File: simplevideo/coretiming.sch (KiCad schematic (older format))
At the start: 9 parts, among them U2 CD74HC40103, U3 CD74HC40103, U6 74HC74, U7 CD74HC40103, U8 CD74HC40103, X1 CXO_DIP8

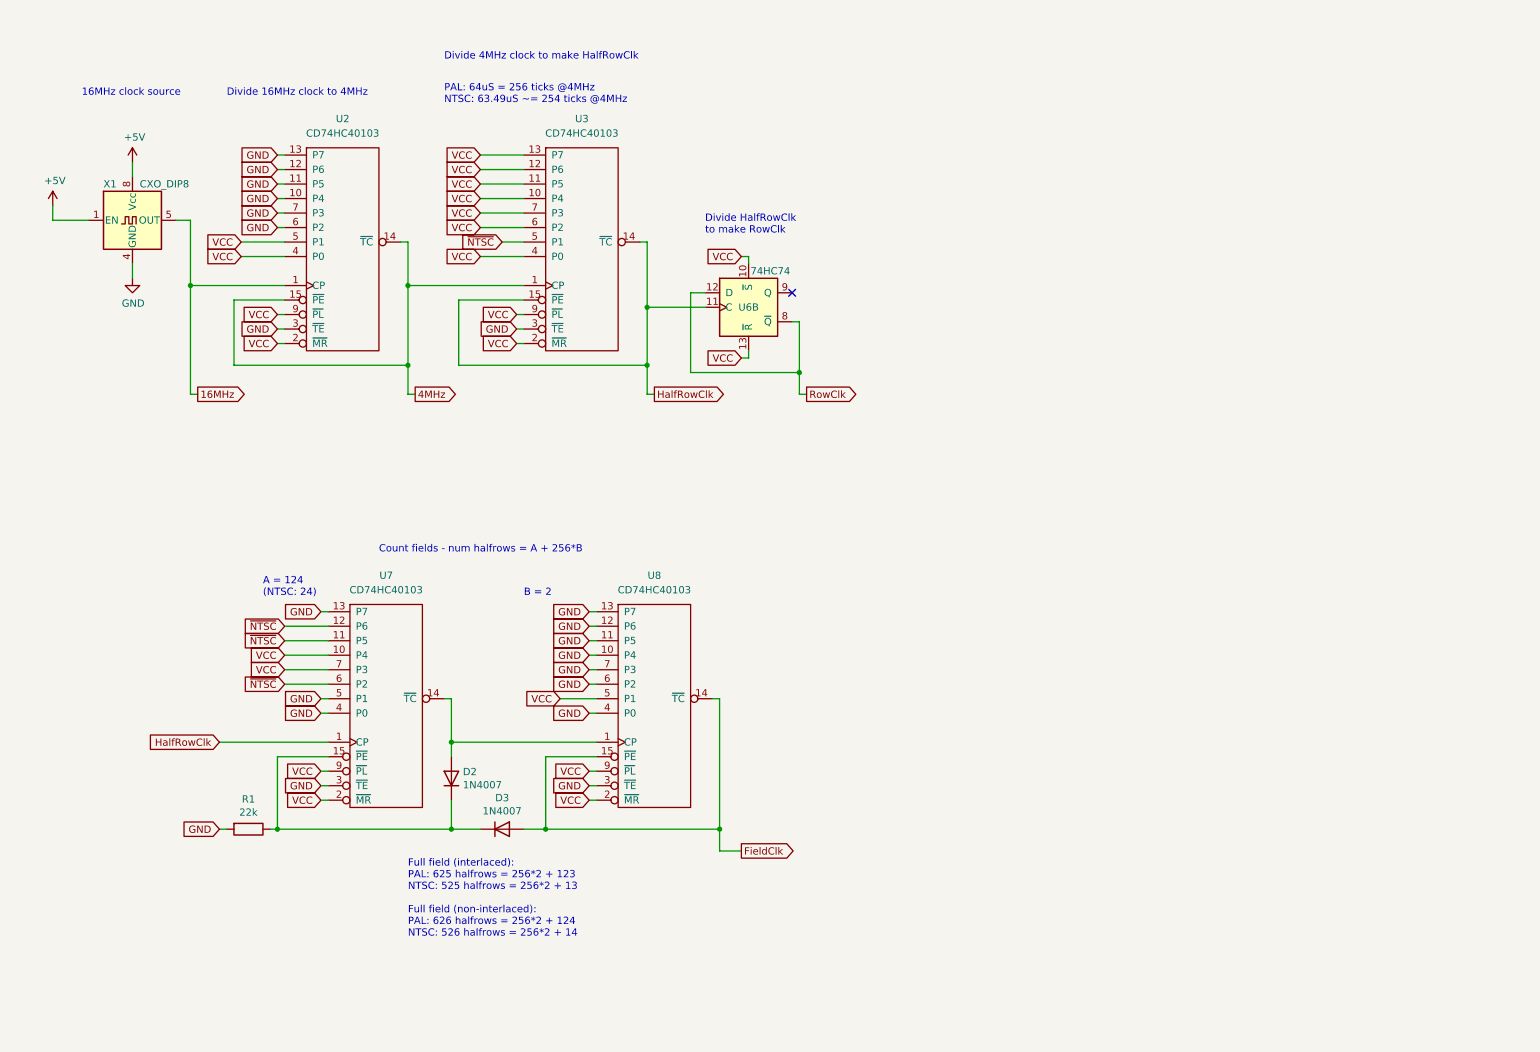
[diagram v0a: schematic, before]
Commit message: Include 6502, ROM, etc in circuit, all laid out together
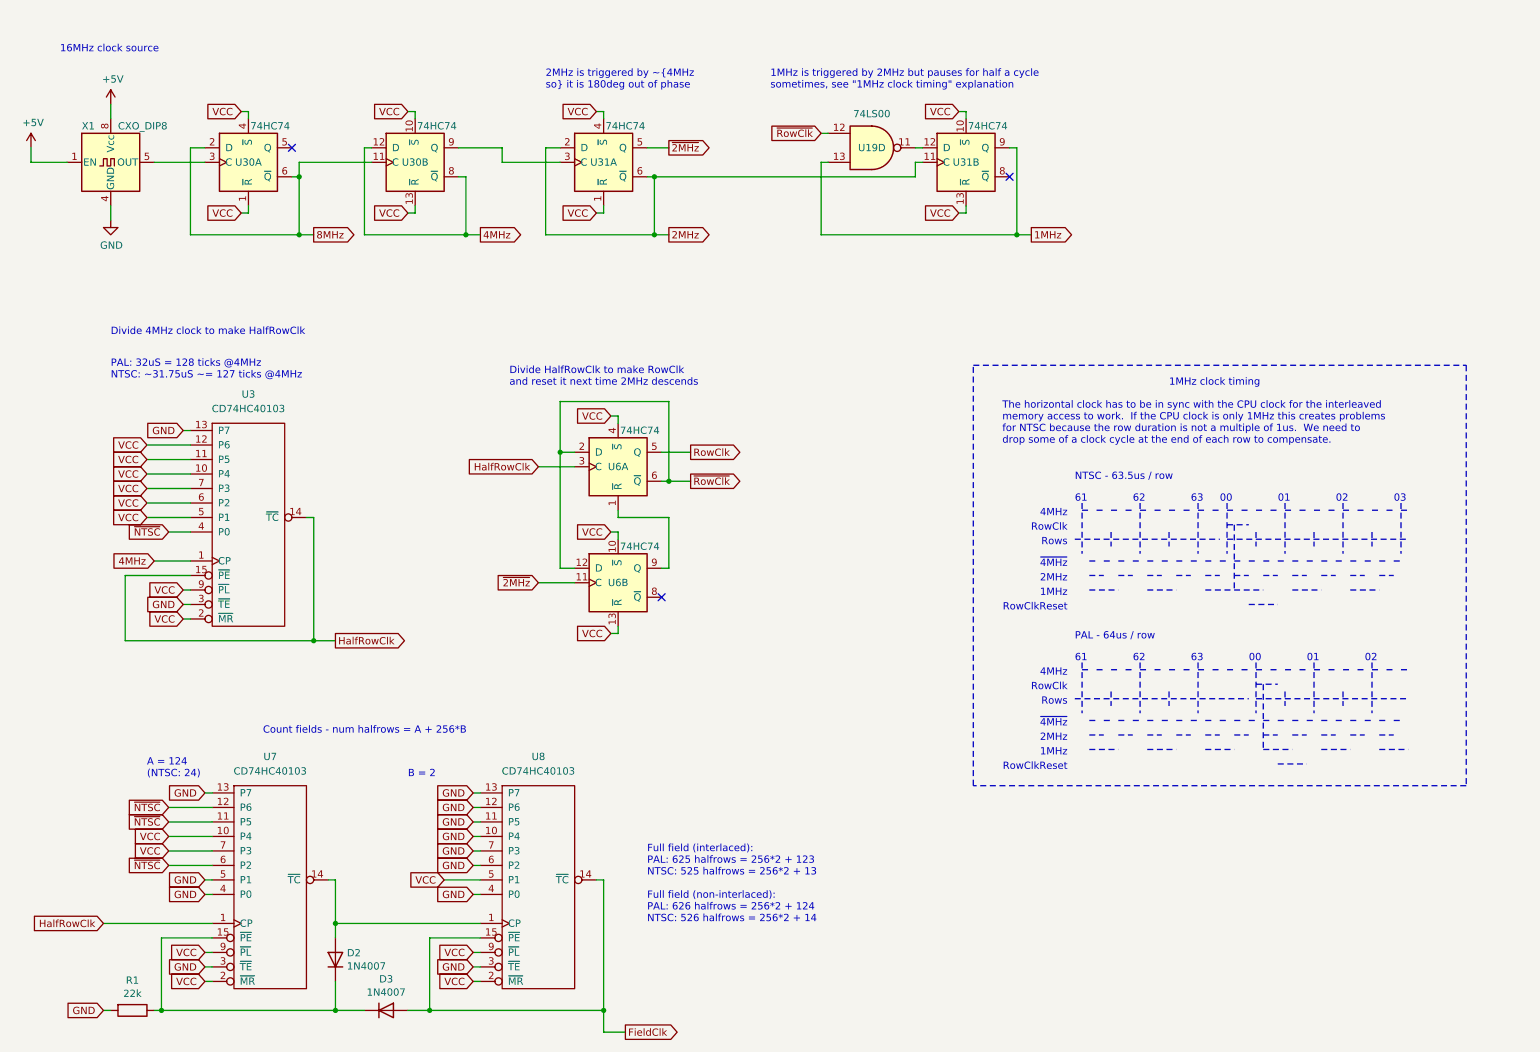
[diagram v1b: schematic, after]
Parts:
- removed U2: CD74HC40103, Package_DIP:DIP-16_W7.62mm, symbol g200kg_CD74HCxx:CD74HC40103
- added U19: 74LS00, Package_DIP:DIP-14_W7.62mm, symbol 74xx:74LS00
- added U30, U31: 74HC74, Package_DIP:DIP-14_W7.62mm, symbol 74xx:74HC74
- added unit 2 of U6
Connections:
- net 4MHz: now also U30.12 (D), U30.8 (~Q)
- net GND: now also U3.13 (P7)
- net HalfRowClk: now also U6.3 (C); no longer U6.11 (C)
- net RowClk: now also U6.5 (Q); no longer U6.12 (D), U6.8 (~Q)
- net VCC: now also U3.5 (P1), U6.4 (~S), U30.1 (~R), U30.10 (~S), U30.13 (~R), U30.4 (~S), U31.1 (~R), U31.10 (~S), U31.13 (~R), U31.4 (~S), U6.10 (~S), U6.13 (~R); no longer U3.13 (P7), U3.4 (P0), U6.10 (~S), U6.13 (~R)
- net ~NTSC: now also U3.4 (P0); no longer U3.5 (P1)
- net 16MHz: no longer names the net of X1.5 (OUT)
- net 16MHz: now also U30.3 (C)
- new net: U6.1 (~R), U6.9 (Q)
- new net: U30.9 (Q), U31.3 (C)
- new net: U19.11, U31.12 (D)
- new net 1MHz: U19.13, U31.9 (Q)
- new net 2MHz: U31.11 (C), U31.2 (D), U31.6 (~Q)
- new net 8MHz: U30.11 (C), U30.2 (D), U30.6 (~Q)
- new net ~2MHz: U31.5 (Q), U6.11 (C)
- new net ~RowClk: U19.12, U6.12 (D), U6.2 (D), U6.6 (~Q)
- no-connect marks 1 -> 3
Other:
- note added: "00"
- note added: "01"
- note added: "02"
- note added: "03"
- note added: "1MHz"
- note added: "1MHz clock timing"
- note added: "1MHz is triggered by 2MHz but pauses for half a cycle\nsometimes, see "1MHz clock timing" explanation"
- note added: "2MHz"
- note added: "2MHz is triggered by ~4MHz\nso it is 180deg out of phase"
- note added: "4MHz"
- note added: "61"
- note added: "62"
- note added: "63"
- note added: "Divide HalfRowClk to make RowClk \nand reset it next time 2MHz descends"
- note added: "NTSC - 63.5us / row"
- note added: "PAL - 64us / row"
- note added: "PAL: 32uS = 128 ticks @4MHz\nNTSC: ~~31.75uS ~~= 127 ticks @4MHz"
- note added: "RowClk"
- note added: "RowClkReset"
- note added: "Rows"
- note added: "The horizontal clock has to be in sync with the CPU clock for the interleaved \nmemory access to work. If the CPU clock is only 1MHz this creates problems\nfor NTSC because the row duration is not a multiple of 1us. We need to \ndrop some of a clock cycle at the end of each row to compensate."
- note added: "~4MHz"
- note removed: "Divide 16MHz clock to 4MHz"
- note removed: "Divide HalfRowClk\nto make RowClk"
- note removed: "PAL: 64uS = 256 ticks @4MHz\nNTSC: 63.49uS ~~= 254 ticks @4MHz"
- moved on the sheet: D2, D3, R1, U3, U7, U8, X1

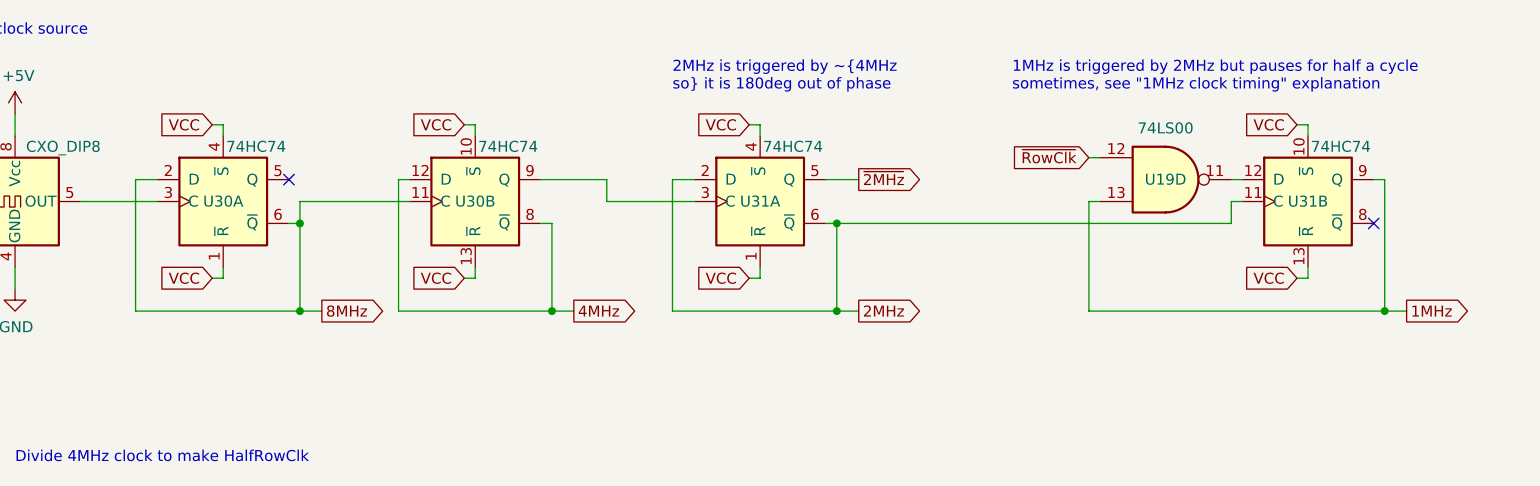
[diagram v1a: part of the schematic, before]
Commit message: New address decoding scheme and complete breadboard layout, should be ready to build
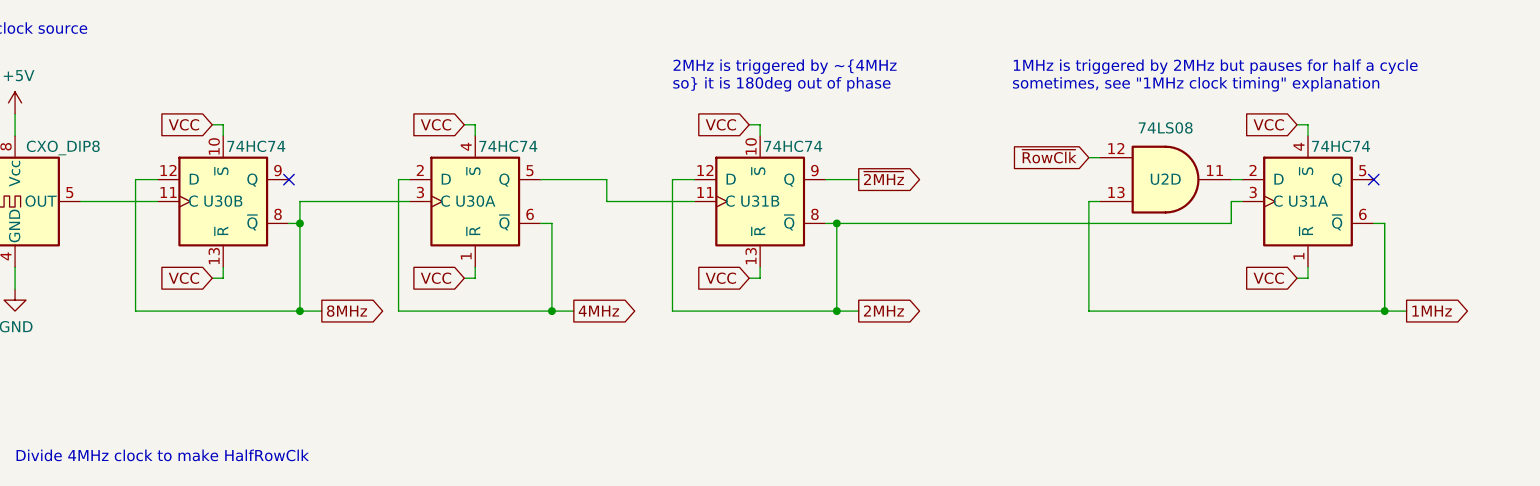
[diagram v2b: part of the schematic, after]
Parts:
- removed U19: 74LS00, Package_DIP:DIP-14_W7.62mm, symbol 74xx:74LS00
- added U2: 74LS08, Package_DIP:DIP-14_W7.62mm, symbol 74xx:74LS08
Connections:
- net 1MHz: now also U31.6 (~Q), U2.13; no longer U31.9 (Q)
- net 2MHz: now also U31.12 (D), U31.3 (C), U31.8 (~Q); no longer U31.11 (C), U31.2 (D), U31.6 (~Q)
- net 4MHz: now also U30.2 (D), U30.6 (~Q); no longer U30.12 (D), U30.8 (~Q)
- net 8MHz: now also U30.12 (D), U30.3 (C), U30.8 (~Q); no longer U30.11 (C), U30.2 (D), U30.6 (~Q)
- net VCC: now also U30.1 (~R), U30.10 (~S), U30.13 (~R), U30.4 (~S), U31.1 (~R), U31.10 (~S), U31.13 (~R), U31.4 (~S); no longer U30.1 (~R), U30.10 (~S), U30.13 (~R), U30.4 (~S), U31.1 (~R), U31.10 (~S), U31.13 (~R), U31.4 (~S)
- net ~2MHz: now also U31.9 (Q); no longer U31.5 (Q)
- net ~RowClk: now also U2.12
- net at X1.5 (OUT): now also U30.11 (C); no longer U30.3 (C)
- new net: U2.11, U31.2 (D)
- new net: U30.5 (Q), U31.11 (C)
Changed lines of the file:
@@
 $Comp
 L 74xx:74HC74 U31
-U 1 1 5F19D9A7
+U 2 1 5F19D9A7
 P 4750 1550
 F 0 "U31" H 4750 1550 50  0000 C CNN
@@
 F 2 "Package_DIP:DIP-14_W7.62mm" H 4750 1550 50  0001 C CNN
 F 3 "74xx/74hc_hct74.pdf" H 4750 1550 50  0001 C CNN
-	1    4750 1550
+	2    4750 1550
 	1    0    0    -1
 $EndComp
@@
 $Comp
 L 74xx:74HC74 U30
-U 1 1 5F5E2F31
+U 2 1 5F5E2F31
 P 2300 1550
 F 0 "U30" H 2300 1550 50  0000 C CNN
@@
 F 2 "Package_DIP:DIP-14_W7.62mm" H 2300 1550 50  0001 C CNN
 F 3 "74xx/74hc_hct74.pdf" H 2300 1550 50  0001 C CNN
-	1    2300 1550
+	2    2300 1550
 	1    0    0    -1
 $EndComp
@@
 $Comp
 L 74xx:74HC74 U30
-U 2 1 5F5E2F40
+U 1 1 5F5E2F40
 P 3450 1550
 F 0 "U30" H 3450 1550 50  0000 C CNN
@@
 F 2 "Package_DIP:DIP-14_W7.62mm" H 3450 1550 50  0001 C CNN
 F 3 "74xx/74hc_hct74.pdf" H 3450 1550 50  0001 C CNN
-	2    3450 1550
+	1    3450 1550
 	1    0    0    -1
 $EndComp
@@
 Text GLabel 7700 2050 2    50   Output ~ 0
 1MHz
-Wire Wire Line
-	7550 1450 7600 1450
 $Comp
 L 74xx:74HC74 U31
-U 2 1 5F1AF2A1
+U 1 1 5F1AF2A1
 P 7250 1550
 F 0 "U31" H 7250 1550 50  0000 C CNN
@@
 F 2 "Package_DIP:DIP-14_W7.62mm" H 7250 1550 50  0001 C CNN
 F 3 "74xx/74hc_hct74.pdf" H 7250 1550 50  0001 C CNN
-	2    7250 1550
+	1    7250 1550
 	1    0    0    -1
 $EndComp
@@
 ~RowClk
 Wire Wire Line
-	7600 2050 7600 1450
+	7600 2050 7600 1650
 Wire Wire Line
 	7600 2050 7700 2050
@@
 Connection ~ 5100 1650
 Connection ~ 7600 2050
-NoConn ~ 7550 1650
 NoConn ~ 5150 4550
 $Comp
-L 74xx:74LS00 U19
-U 4 1 5FF126B3
+L 74xx:74LS08 U2
+U 4 1 5F0D1BCB
 P 6600 1450
-F 0 "U19" H 6600 1450 50  0000 C CNN
-F 1 "74LS00" H 6600 1684 50  0000 C CNN
+F 0 "U2" H 6600 1450 50  0000 C CNN
+F 1 "74LS08" H 6600 1684 50  0000 C CNN
 F 2 "Package_DIP:DIP-14_W7.62mm" H 6600 1450 50  0001 C CNN
-F 3 "http://www.ti.com/lit/gpn/sn74ls00" H 6600 1450 50  0001 C CNN
+F 3 "http://www.ti.com/lit/gpn/sn74LS08" H 6600 1450 50  0001 C CNN
 	4    6600 1450
 	1    0    0    -1
 $EndComp
+Wire Wire Line
+	7550 1650 7600 1650
+NoConn ~ 7550 1450
 $EndSCHEMATC

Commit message: Fixed various issues discovered during building and testing
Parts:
- added U19: 74LS00, Package_DIP:DIP-14_W7.62mm, symbol 74xx:74LS00
- D2, D3: value 1N4007 -> 1N4148
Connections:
- net RowClk: now also U6.12 (D), U19.12
- net VCC: now also U6.1 (~R)
- net ~RowClk: no longer U2.12, U6.12 (D)
- net at U6.9 (Q): no longer U6.1 (~R)
- net ~DelayedRowClk: now reaches U6.8 (~Q)
- net ~DelayedRowClk: now also U19.13
- new net: U19.11, U2.12
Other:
- note added: "13.5MHz"
- note added: "216 @6.75MHz"
- note added: "27MHz"
- note added: "6.75MHz"
- note added: "Delayed RowClk to help detect when it starts"
- note added: "DelayedRowClk"
- note added: "Divide HalfRowClk to make RowClk"
- note added: "The horizontal clock has to be in sync with the CPU clock for the interleaved \nmemory access to work. If the CPU clock is only 1MHz this creates problems\nfor NTSC because the row duration is not a multiple of 1us. We need to \ndrop some of a clock cycle at the end of each row to compensate.\n\nSo 1MHz clocks on the rising edge of 2MHz, to its inverse OR \n(RowClk && !DelayedRowClk)"
- note removed: "Divide HalfRowClk to make RowClk \nand reset it next time 2MHz descends"
- note removed: "The horizontal clock has to be in sync with the CPU clock for the interleaved \nmemory access to work. If the CPU clock is only 1MHz this creates problems\nfor NTSC because the row duration is not a multiple of 1us. We need to \ndrop some of a clock cycle at the end of each row to compensate."
- moved on the sheet: U2D, U31A, U6A, U6B
